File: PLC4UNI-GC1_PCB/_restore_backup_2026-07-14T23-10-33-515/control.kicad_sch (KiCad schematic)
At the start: 22 parts, among them J1 Conn_02x08_Odd_Even, SW1 TS-1088-AR02016, U1 ESP32-S3-WROOM-1, U10 ADS1115IDGS, U4 RS485-PROTECT

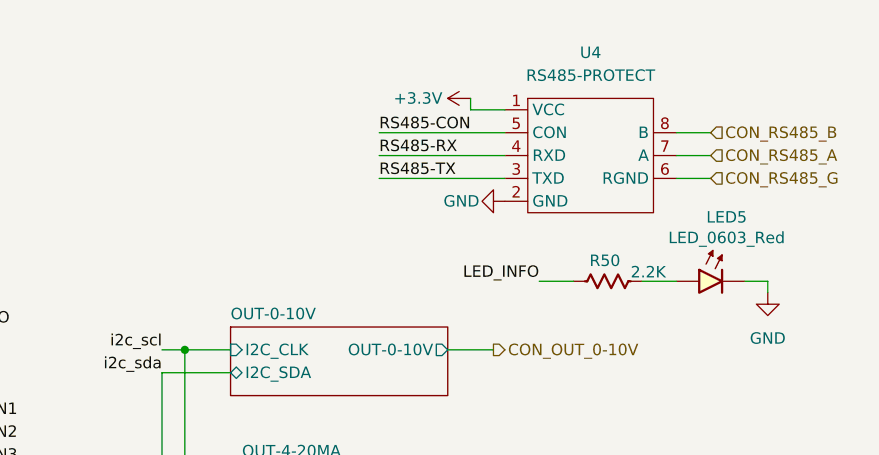
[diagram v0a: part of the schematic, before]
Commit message: edge.cuts update
areglo d e cortes de placa estaban desalineados
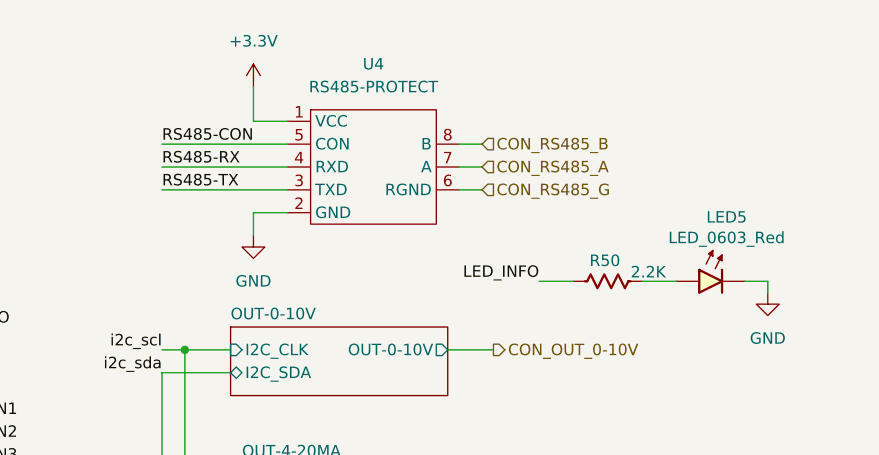
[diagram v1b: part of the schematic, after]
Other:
- moved on the sheet: U4
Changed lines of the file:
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@@
 	(wire
 		(pts
-			(xy 227.33 25.4) (xy 241.3 25.4)
+			(xy 203.2 26.67) (xy 217.17 26.67)
 		)
 		(stroke
@@
 	(wire
 		(pts
-			(xy 227.33 27.94) (xy 241.3 27.94)
+			(xy 203.2 29.21) (xy 217.17 29.21)
 		)
 		(stroke
@@
 	(wire
 		(pts
-			(xy 260.35 30.48) (xy 264.16 30.48)
+			(xy 236.22 31.75) (xy 238.76 31.75)
 		)
 		(stroke
@@
 	(wire
 		(pts
-			(xy 260.35 25.4) (xy 264.16 25.4)
+			(xy 236.22 26.67) (xy 238.76 26.67)
 		)
 		(stroke
@@
 	(wire
 		(pts
+			(xy 217.17 34.29) (xy 213.36 34.29)
+		)
+		(stroke
+			(width 0)
+			(type default)
+		)
+	)
+	(wire
+		(pts
 			(xy 71.12 35.56) (xy 90.17 35.56)
 		)
@@
 	(wire
 		(pts
-			(xy 260.35 27.94) (xy 264.16 27.94)
+			(xy 236.22 29.21) (xy 238.76 29.21)
 		)
 		(stroke
@@
 	(wire
 		(pts
+			(xy 213.36 34.29) (xy 213.36 36.83)
+		)
+		(stroke
+			(width 0)
+			(type default)
+		)
+	)
+	(wire
+		(pts
 			(xy 71.12 31.75) (xy 71.12 35.56)
 		)
@@
 	(wire
 		(pts
-			(xy 227.33 30.48) (xy 241.3 30.48)
+			(xy 203.2 31.75) (xy 217.17 31.75)
 		)
 		(stroke
@@
 	(wire
 		(pts
-			(xy 241.3 22.86) (xy 237.49 22.86)
+			(xy 217.17 24.13) (xy 213.36 24.13)
 		)
 		(stroke
@@
 	(wire
 		(pts
-			(xy 237.49 21.59) (xy 237.49 22.86)
+			(xy 213.36 20.32) (xy 213.36 24.13)
 		)
 		(stroke
@@
 	)
 	(label "RS485-TX"
-		(at 227.33 30.48 0)
+		(at 203.2 31.75 0)
 		(effects
 			(font
@@
 	)
 	(label "RS485-CON"
-		(at 227.33 25.4 0)
+		(at 203.2 26.67 0)
 		(effects
 			(font
@@
 	)
 	(label "RS485-RX"
-		(at 227.33 27.94 0)
+		(at 203.2 29.21 0)
 		(effects
 			(font
@@
 	(hierarchical_label "CON_RS485_G"
 		(shape input)
-		(at 264.16 30.48 0)
+		(at 238.76 31.75 0)
 		(effects
 			(font
@@
 	(hierarchical_label "CON_RS485_A"
 		(shape input)
-		(at 264.16 27.94 0)
+		(at 238.76 29.21 0)
 		(effects
 			(font
@@
 	(hierarchical_label "CON_RS485_B"
 		(shape input)
-		(at 264.16 25.4 0)
+		(at 238.76 26.67 0)
 		(effects
 			(font
@@
 	(symbol
 		(lib_id "power:+3.3V")
-		(at 237.49 21.59 90)
+		(at 213.36 20.32 0)
 		(unit 1)
 		(body_style 1)
@@
 		(in_pos_files yes)
 		(dnp no)
+		(fields_autoplaced yes)
 		(property "Reference" "#PWR019"
-			(at 241.3 21.59 0)
+			(at 213.36 24.13 0)
 			(hide yes)
 			(show_name no)
@@
 		)
 		(property "Value" "+3.3V"
-			(at 231.648 21.59 90)
+			(at 213.36 15.24 0)
 			(show_name no)
 			(do_not_autoplace no)
@@
 		)
 		(property "Footprint" ""
-			(at 237.49 21.59 0)
+			(at 213.36 20.32 0)
 			(hide yes)
 			(show_name no)
@@
 		)
 		(property "Datasheet" ""
-			(at 237.49 21.59 0)
+			(at 213.36 20.32 0)
 			(hide yes)
 			(show_name no)
@@
 		)
 		(property "Description" "Power symbol creates a global label with name \"+3.3V\""
-			(at 237.49 21.59 0)
+			(at 213.36 20.32 0)
 			(hide yes)
 			(show_name no)
@@
 	(symbol
 		(lib_id "power:GND")
-		(at 241.3 33.02 270)
+		(at 213.36 36.83 0)
 		(unit 1)
 		(body_style 1)
@@
 		(in_pos_files yes)
 		(dnp no)
+		(fields_autoplaced yes)
 		(property "Reference" "#PWR020"
-			(at 234.95 33.02 0)
+			(at 213.36 43.18 0)
 			(hide yes)
 			(show_name no)
@@
 		)
 		(property "Value" "GND"
-			(at 236.474 33.02 90)
+			(at 213.36 41.91 0)
 			(show_name no)
 			(do_not_autoplace no)
@@
 		)
 		(property "Footprint" ""
-			(at 241.3 33.02 0)
+			(at 213.36 36.83 0)
 			(hide yes)
 			(show_name no)
@@
 		)
 		(property "Datasheet" ""
-			(at 241.3 33.02 0)
+			(at 213.36 36.83 0)
 			(hide yes)
 			(show_name no)
@@
 		)
 		(property "Description" "Power symbol creates a global label with name \"GND\" , ground"
-			(at 241.3 33.02 0)
+			(at 213.36 36.83 0)
 			(hide yes)
 			(show_name no)
@@
 	(symbol
 		(lib_id "MG_CONNECTORS:RS485-PROTECT")
-		(at 247.65 27.94 0)
+		(at 223.52 29.21 0)
 		(unit 1)
 		(body_style 1)
@@
 		(fields_autoplaced yes)
 		(property "Reference" "U4"
-			(at 250.825 16.51 0)
+			(at 226.695 17.78 0)
 			(show_name no)
 			(do_not_autoplace no)
@@
 		)
 		(property "Value" "RS485-PROTECT"
-			(at 250.825 19.05 0)
+			(at 226.695 20.32 0)
 			(show_name no)
 			(do_not_autoplace no)
@@
 		)
 		(property "Footprint" "MG_footprints:RS-485-PROTECT"
-			(at 247.65 27.94 0)
+			(at 223.52 29.21 0)
 			(hide yes)
 			(show_name no)
@@
 		)
 		(property "Datasheet" ""
-			(at 247.65 27.94 0)
+			(at 223.52 29.21 0)
 			(hide yes)
 			(show_name no)
@@
 		)
 		(property "Description" ""
-			(at 247.65 27.94 0)
+			(at 223.52 29.21 0)
 			(hide yes)
 			(show_name no)
@@
 		)
 		(property "Part Number" "RS-485-PROTECT"
-			(at 247.65 27.94 0)
+			(at 223.52 29.21 0)
 			(hide yes)
 			(show_name no)
@@
 		)
 		(property "Manufacturer" "Manicato Group"
-			(at 247.65 27.94 0)
+			(at 223.52 29.21 0)
 			(hide yes)
 			(show_name no)
@@
 		)
 		(property "PART_NUMBER" ""
-			(at 247.65 27.94 0)
+			(at 223.52 29.21 0)
 			(hide yes)
 			(show_name no)
@@
 		)
 		(property "LCSC Part #" ""
-			(at 247.65 27.94 0)
+			(at 223.52 29.21 0)
 			(hide yes)
 			(show_name no)
@@
 		)
 		(property "VOL" ""
-			(at 247.65 27.94 0)
+			(at 223.52 29.21 0)
 			(show_name no)
 			(do_not_autoplace no)
@@
 		)
 		(property "TOL" ""
-			(at 247.65 27.94 0)
+			(at 223.52 29.21 0)
 			(show_name no)
 			(do_not_autoplace no)
